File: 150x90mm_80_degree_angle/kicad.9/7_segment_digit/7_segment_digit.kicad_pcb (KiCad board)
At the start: 2 copper layers, 90 x 150 mm, 15 parts, among them X1 PLS-10

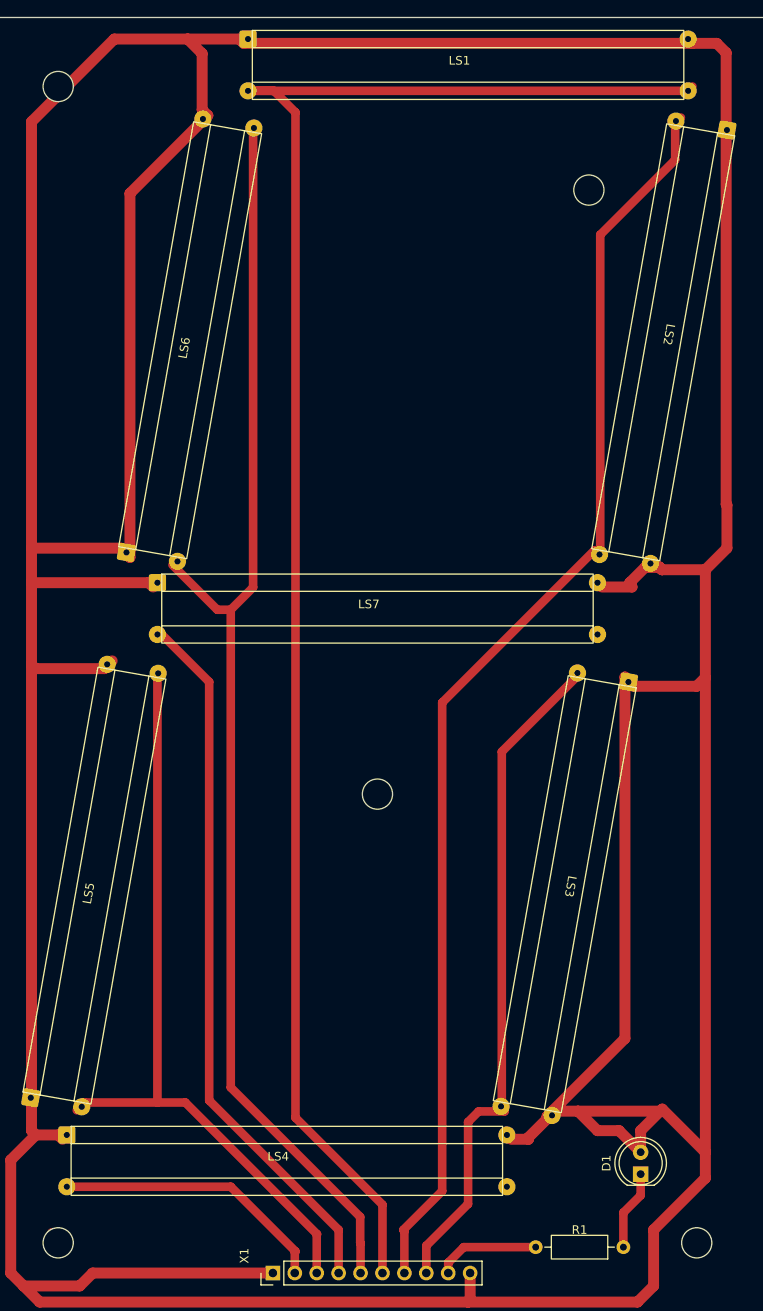
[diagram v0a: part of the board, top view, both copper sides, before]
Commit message: Добавил символ и посадочную площадку СИД SMD 5050. Обновил схему и ПП.
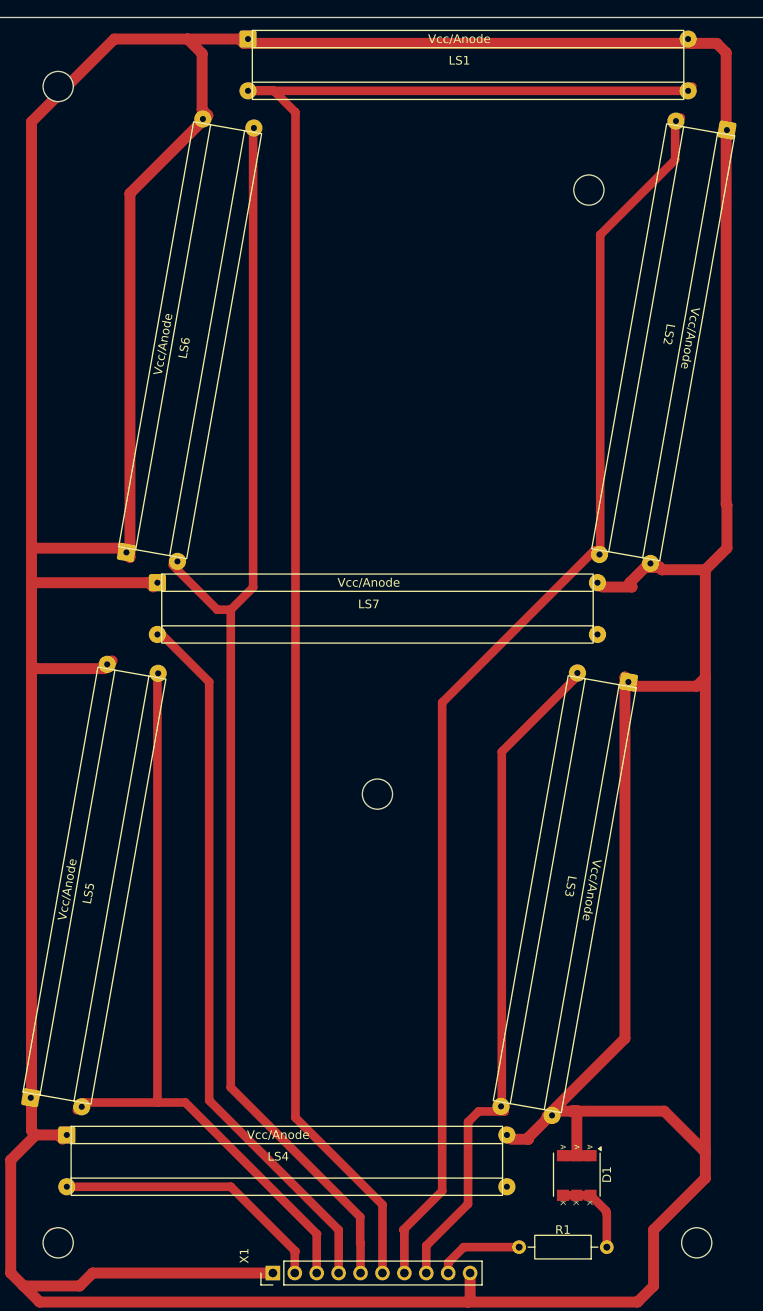
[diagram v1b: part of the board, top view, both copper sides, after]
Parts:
- D1: value LED -> ~; footprint LED_THT:LED_D5.0mm -> led_strip:LED_SMD_5050_6
- moved D1 7.40 mm to (122.6, 157.6), turned to -90 degrees
- moved R1 1.92 mm to (126.1, 166.0)
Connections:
- D1 pad 1: /1 -> VCC
- D1 pad 2: VCC -> /1
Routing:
- net VCC: track 701.3 -> 696.1 mm
- net /SEG_DP: track 12.1 -> 10.2 mm
- net /1: track 9.29 -> 9.98 mm
